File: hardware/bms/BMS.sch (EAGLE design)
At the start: 128 parts, among them IC1 LM358D, Q1 FDY102PZ, Q10 FDY102PZ, Q11 FDY102PZ, Q12 FDY102PZ, Q2 FDY102PZ, Q3 FDY102PZ, Q4 FDY102PZ, Q5 FDY102PZ, Q6 FDY102PZ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

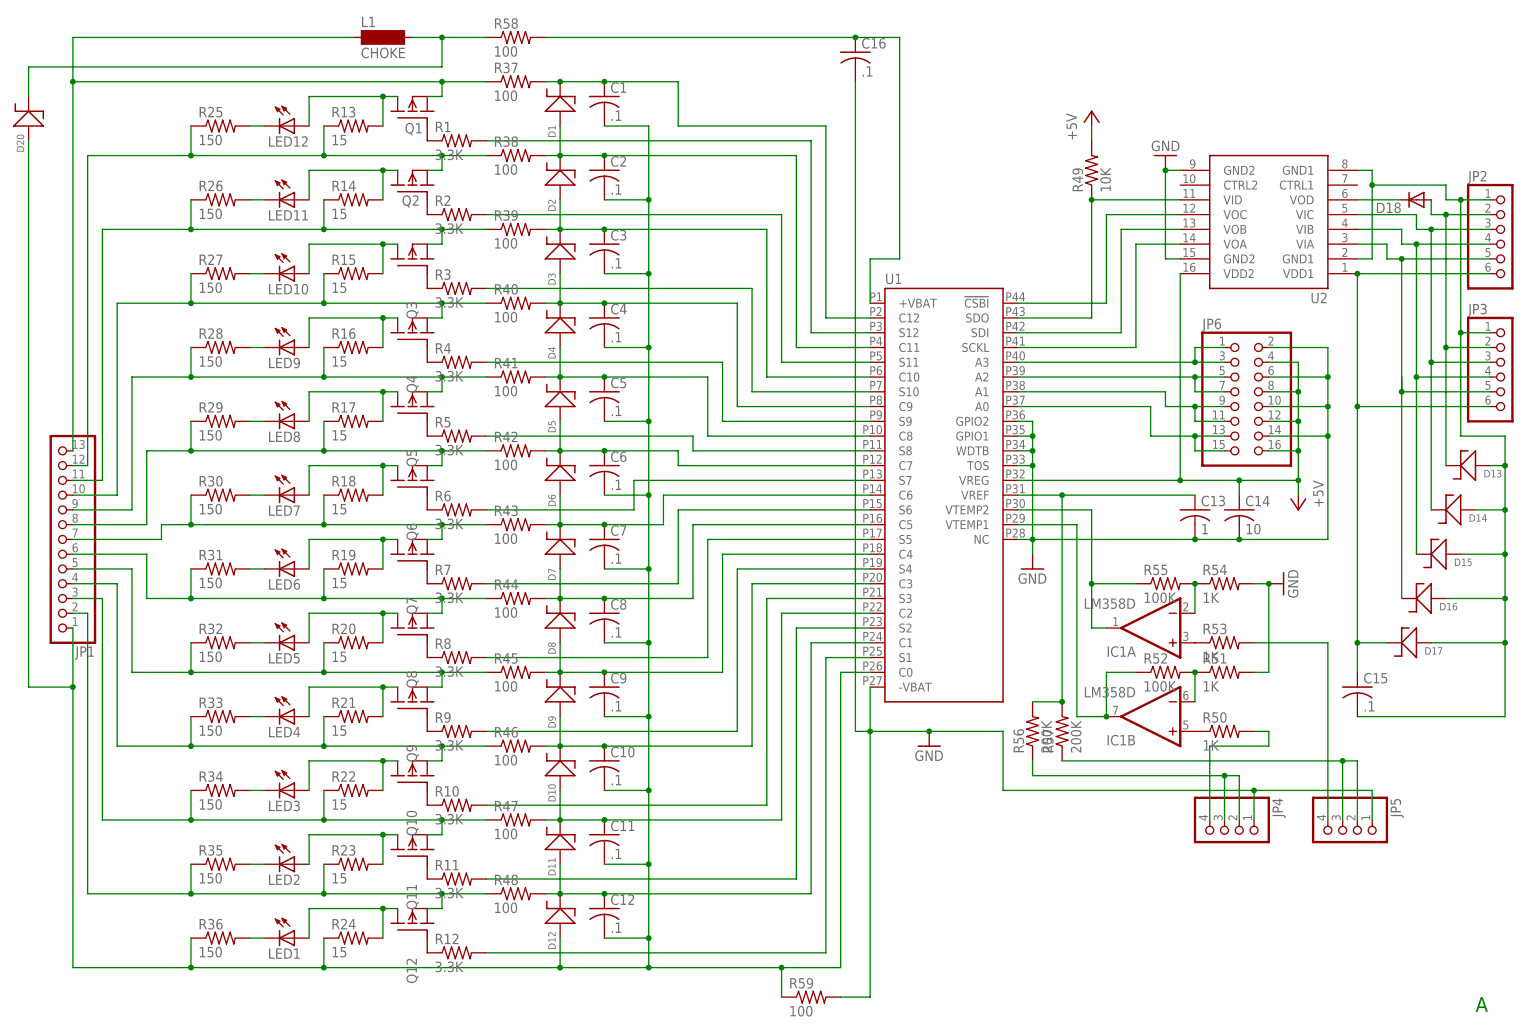
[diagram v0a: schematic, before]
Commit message: First completed version of the BMS board schematic and layout for Martin to check and comment on. By Richard Weaver 2/16/13
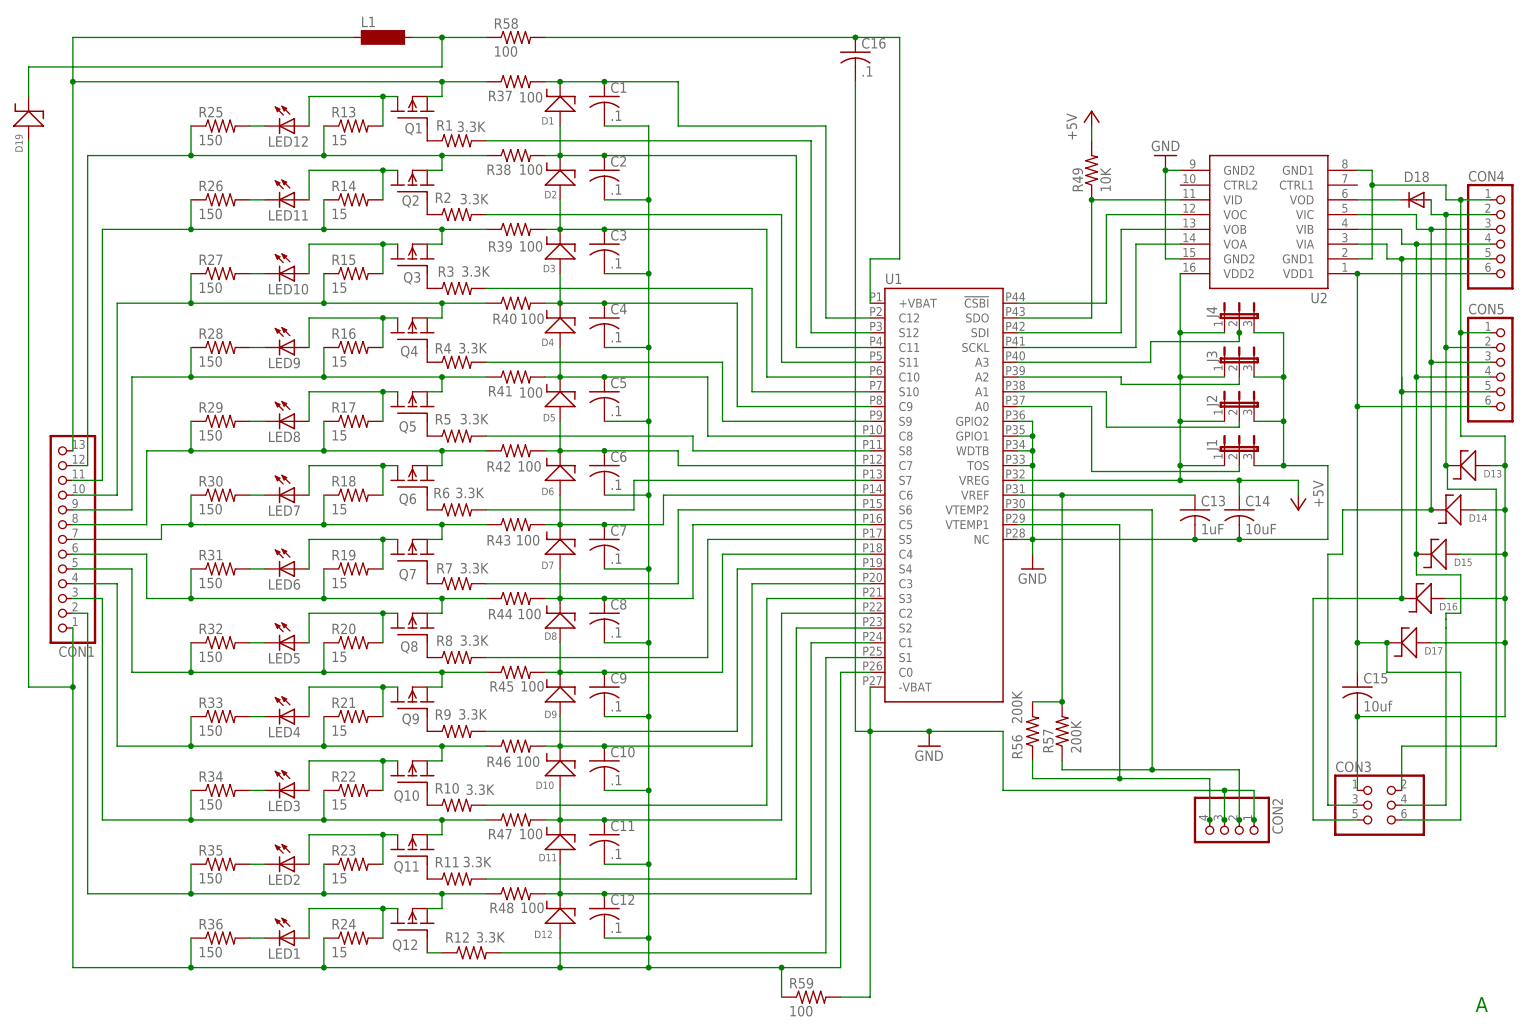
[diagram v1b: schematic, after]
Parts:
- removed D20: (no value), Richard1:PDZ7.5B
- removed IC1: LM358D, linear:LM358D
- removed JP5: (no value), pinhead:PINHD-1X4/90
- removed JP6: (no value), pinhead:PINHD-2X8
- removed R50, R51, R53, R54: 1K, rcl:R-US_R0603
- removed R52, R55: 100K, rcl:R-US_R0603
- added CON3: (no value), pinhead:PINHD-2X3/90
- added D19: MMSZ5265BTIG, Richard1:MMSZ5265BTIG
- added J1, J2, J3, J4: (no value), jumper:JP2E
- C13: value 1 -> 1uF
- C14: value 10 -> 10uF
- C15: value .1 -> 10uf
- D17: DIGIKEY (none) -> 568-
- D18: value DIODE10603 -> DIODE0603; device Richard1:DIODE10603 -> Richard1:DIODE0603
- renumbered JP1 to CON1, JP2 to CON4, JP3 to CON5, JP4 to CON2
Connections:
- removed net N$80: JP6.1, JP6.3, U1.A3
- removed net N$81: JP6.11, JP6.9, U1.A1
- removed net N$82: JP6.13, JP6.15, U1.A0
- removed net N$87: CON4.2, CON5.2, D13.1, D18.A
- removed net N$92: IC1A.+IN, R53.1
- removed net N$93: IC1A.-IN, R54.1, R55.2
- removed net N$94: JP5.2, JP5.3, R57.1
- removed net N$95: CON2.2, CON2.3, R56.1
- removed net N$98: JP5.4, R53.2
- removed net N$99: CON2.4, R50.2
- new net N$25: J3.2, U1.A2
- new net N$45: J1.2, U1.A0
- net +5V: now also J1.1, J2.1, J3.1, J4.1; no longer JP6.12, JP6.16, JP6.4, JP6.8
- net GND: now also CON2.3, J1.3, J2.3, J3.3, J4.3; no longer JP5.1, JP6.10, JP6.14, JP6.2, JP6.6, R51.2, R54.2
- net N$102: now also D19.1; no longer D20.1
- net N$13: now also D19.2; no longer D20.2
- net N$57: now also CON3.2, CON4.2, CON5.2, D13.1, D18.A; no longer IC1B.+IN, R50.1
- net N$83: now also CON3.5
- net N$84: now also J2.2, U1.A1; no longer JP6.5, JP6.7, U1.A2
- net N$85: now also CON3.4
- net N$86: now also CON3.3
- net N$88: now also CON3.1
- net N$90: now also CON3.6
- net N$91: now also J4.2, U1.A3; no longer IC1B.-IN, R51.1, R52.2
- net N$96: now also CON2.4, R56.1; no longer IC1B.OUT, R52.1
- net N$97: now also CON2.2, R57.1; no longer IC1A.OUT, R55.1
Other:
- moved on the sheet: R12

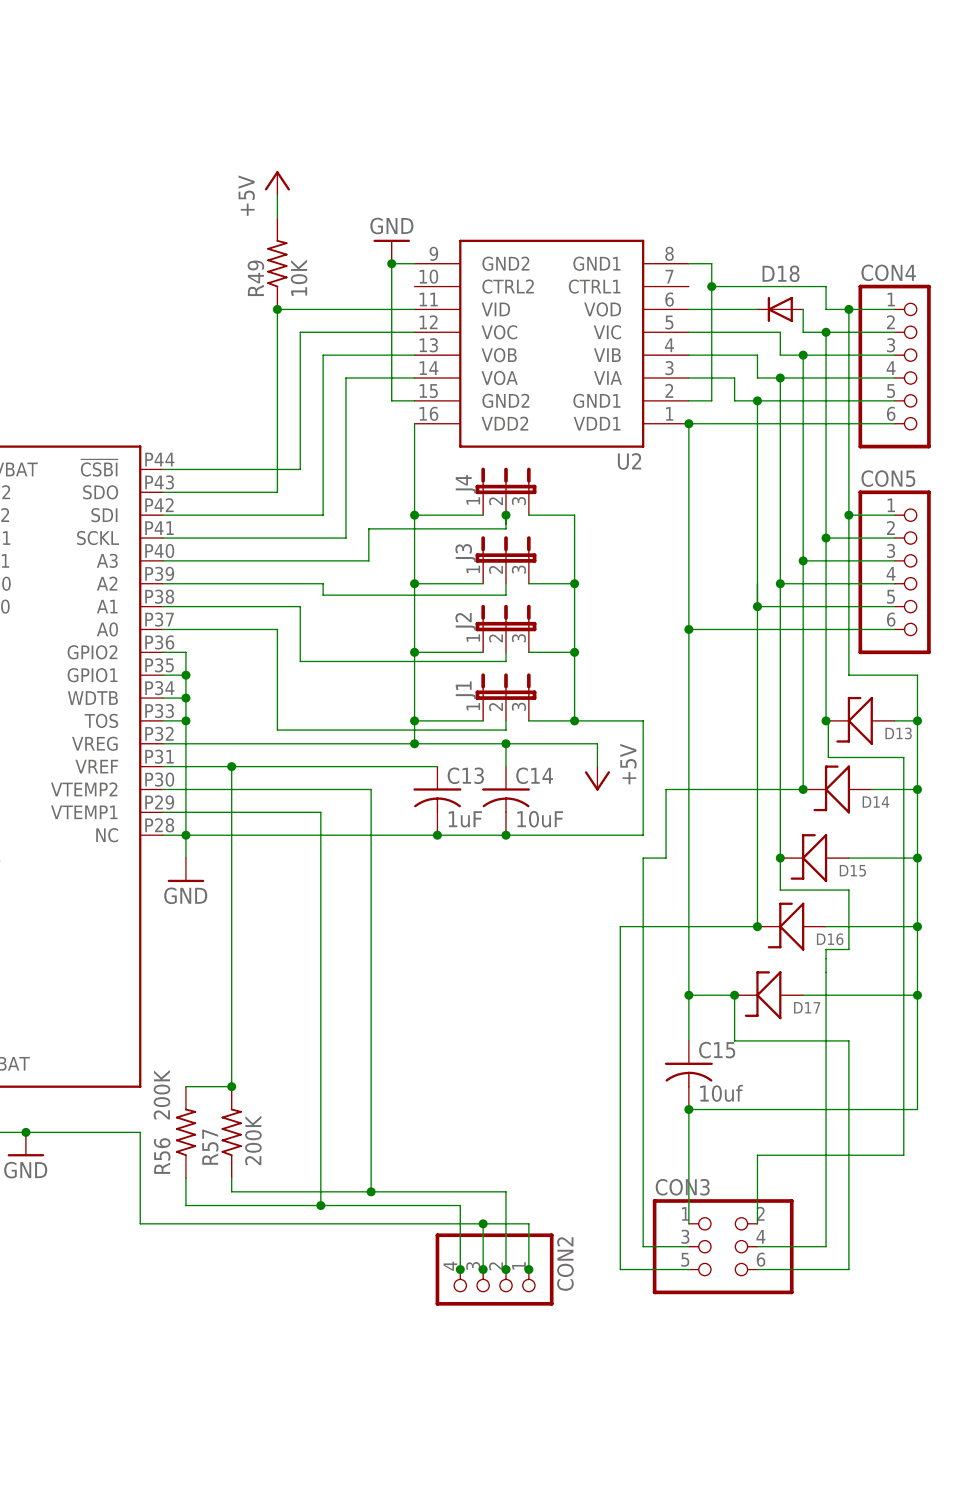
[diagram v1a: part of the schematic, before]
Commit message: Update ground planes, fix misc. route alignment, add decoupling capacitor for '1411. Add ESD protection diode array.
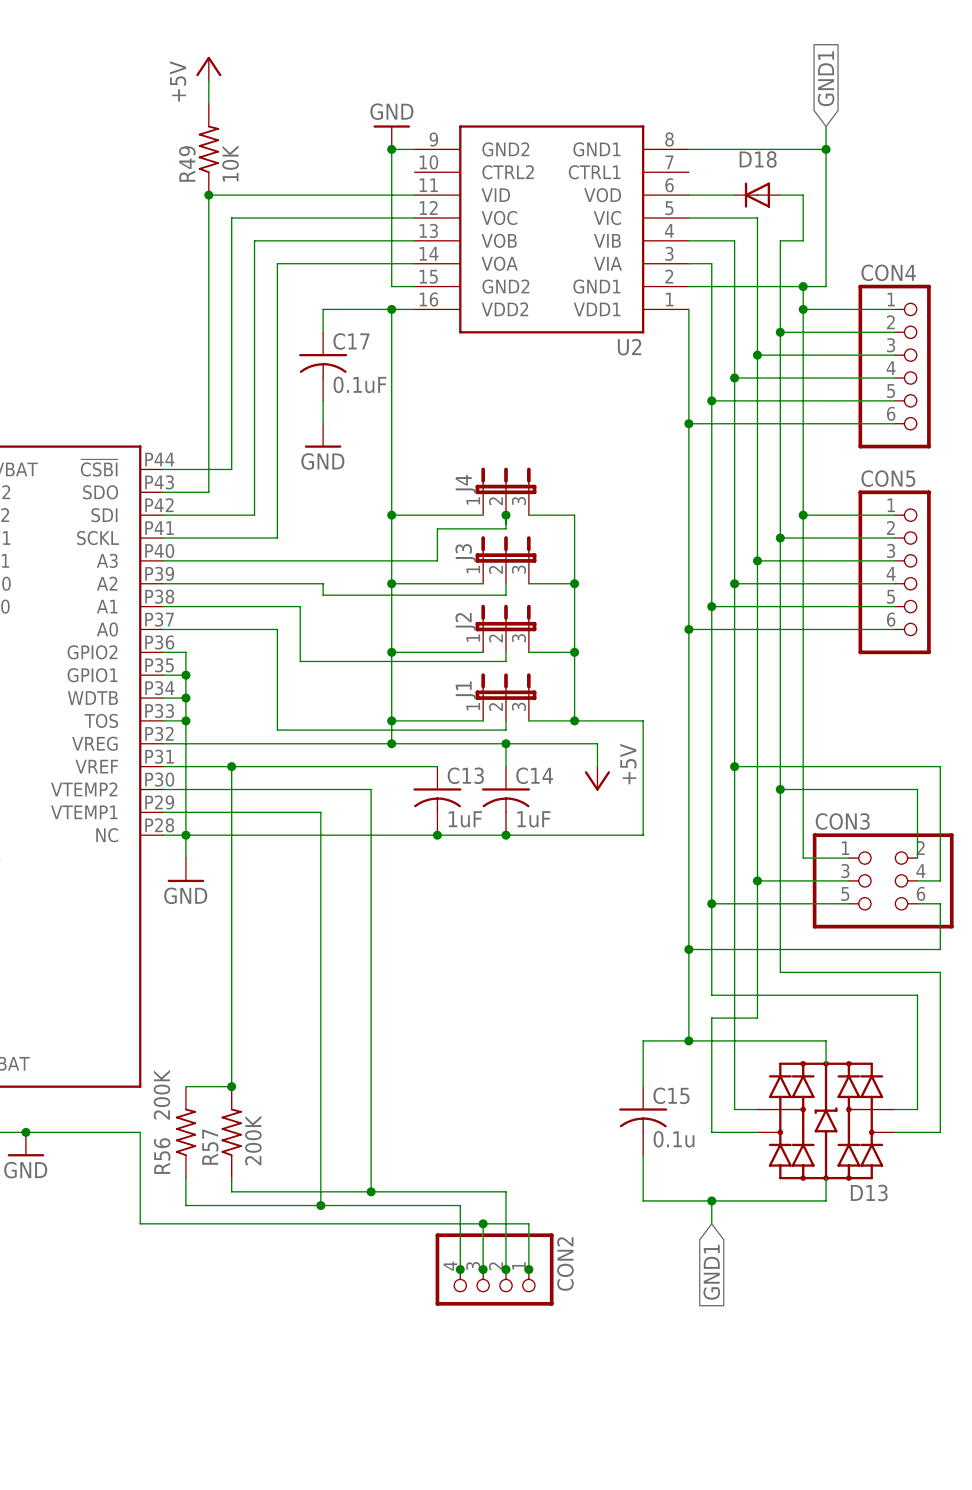
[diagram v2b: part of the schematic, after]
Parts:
- removed D14, D15, D16, D17: (no value), Richard1:PDZ7.5B
- added C17: 0.1uF, rcl:C-USC0603
- C14: value 10uF -> 1uF
- C15: value 10uf -> 0.1u
- D13: device Richard1:PDZ7.5B -> m_diode:TPD4E001DBV
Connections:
- net N$100 renamed +VBAT
- net N$79 renamed VREF
- removed net N$88: C15.2, CON3.1, CON4.1, CON5.1, D13.2, D14.2, D15.2, D16.2, D17.2, U2.GND1@1, U2.GND1@2
- new net GND1: C15.2, CON3.1, CON4.1, CON5.1, D13.GND, U2.GND1@1, U2.GND1@2
- net +5V: now also C17.1
- net GND: now also C17.2
- net N$57: now also D13.IO4; no longer D13.1
- net N$83: now also D13.IO3; no longer D16.1
- net N$85: now also D13.IO2; no longer D15.1
- net N$86: now also D13.IO1; no longer D14.1
- net N$90: now also D13.VCC; no longer D17.1
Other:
- moved on the sheet: C15, CON3, D18, R49, U2
